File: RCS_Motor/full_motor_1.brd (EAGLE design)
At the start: 25.7 x 21.9 mm, 15 parts, among them IC1 ILD213T, T1 2N2222

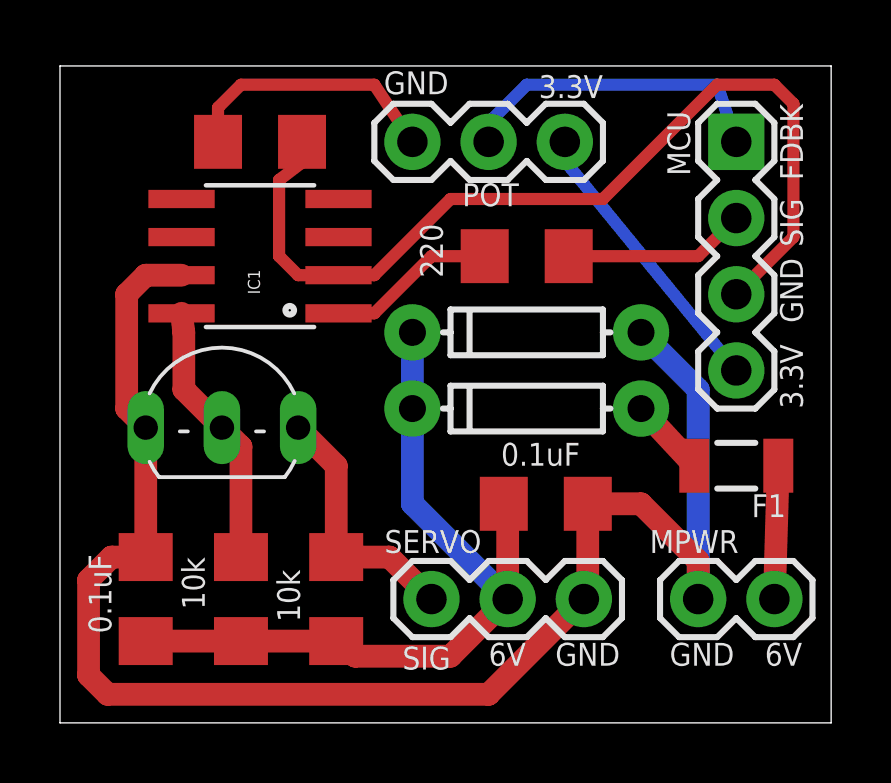
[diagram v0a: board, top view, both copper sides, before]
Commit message: Updated board file
Fixed clearance
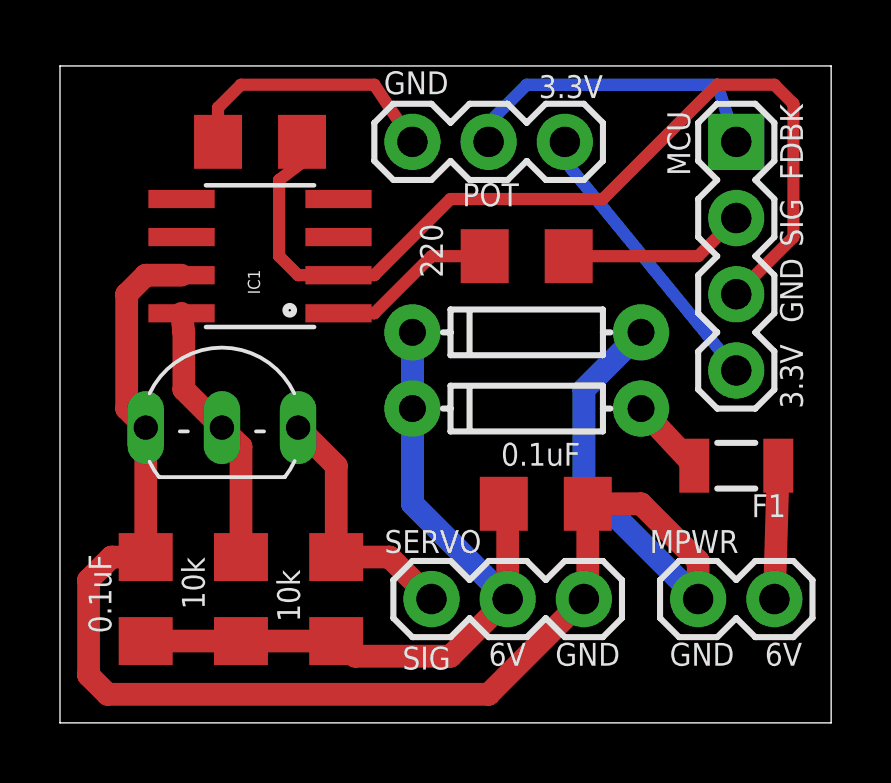
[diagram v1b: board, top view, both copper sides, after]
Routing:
- net GND_MOTOR: track 53.2 -> 54.8 mm
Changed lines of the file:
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@@
 <wire x1="30.61" y1="22.225" x2="32.385" y2="22.225" width="0.759459375" layer="1"/>
 <wire x1="34.29" y1="20.32" x2="34.29" y2="19.05" width="0.759459375" layer="1"/>
-<wire x1="32.385" y1="27.94" x2="34.29" y2="26.035" width="0.759459375" layer="16"/>
-<wire x1="34.29" y1="26.035" x2="34.29" y2="19.05" width="0.759459375" layer="16"/>
 <wire x1="15.875" y1="24.765" x2="15.24" y2="25.4" width="0.759459375" layer="1"/>
 <wire x1="15.24" y1="25.4" x2="15.24" y2="29.21" width="0.759459375" layer="1"/>
@@
 <wire x1="15.875" y1="29.845" x2="17.0688" y2="29.845" width="0.759459375" layer="1"/>
 <wire x1="32.385" y1="22.225" x2="34.29" y2="20.32" width="0.759459375" layer="1"/>
+<wire x1="32.385" y1="27.94" x2="30.48" y2="26.035" width="0.759459375" layer="16"/>
+<wire x1="30.48" y1="26.035" x2="30.48" y2="22.86" width="0.759459375" layer="16"/>
+<wire x1="30.48" y1="22.86" x2="34.29" y2="19.05" width="0.759459375" layer="16"/>
 </signal>
 <signal name="N$3">
